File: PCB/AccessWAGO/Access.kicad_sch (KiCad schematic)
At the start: 82 parts, among them J1 USB-C, J2 NFC, J3 I/O, J4 TC2030-USB-NL-DS, J5 NFC, J6 GND, J7 12V, J8 DOOR, J9 I/O, Q2 PMF250XNEX, SW1 ESE13V01A, U1 MD8942, U10 ESP32-S3-MINI-1, U2 MD8942, U8 G3VM-41GR8

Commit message: Silkscreen, and 21
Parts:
- added J10: Reset, RevK:AA-Pad, symbol Connector_Generic:Conn_01x02
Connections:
- net GND: now also J10.1 (Pin_1)
- net at U10.25 (GPIO21): now also J10.2 (Pin_2)
- no-connect marks 25 -> 24
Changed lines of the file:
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@@
 	)
 	(no_connect
-		(at 39.37 102.87)
-	)
-	(no_connect
 		(at 39.37 69.85)
 	)
@@
 	(wire
 		(pts
+			(xy 30.48 102.87) (xy 39.37 102.87)
+		)
+		(stroke
+			(width 0)
+			(type default)
+		)
+	)
+	(wire
+		(pts
 			(xy 128.905 140.97) (xy 128.905 148.59)
 		)
@@
 	)
 	(symbol
+		(lib_id "power:GND")
+		(at 30.48 105.41 90)
+		(unit 1)
+		(exclude_from_sim no)
+		(in_bom yes)
+		(on_board yes)
+		(dnp no)
+		(fields_autoplaced yes)
+		(property "Reference" "#PWR09"
+			(at 36.83 105.41 0)
+			(effects
+				(font
+					(size 1.27 1.27)
+				)
+				(hide yes)
+			)
+		)
+		(property "Value" "GND"
+			(at 33.655 105.41 90)
+			(effects
+				(font
+					(size 1.27 1.27)
+				)
+				(justify right)
+			)
+		)
+		(property "Footprint" ""
+			(at 30.48 105.41 0)
+			(effects
+				(font
+					(size 1.27 1.27)
+				)
+				(hide yes)
+			)
+		)
+		(property "Datasheet" ""
+			(at 30.48 105.41 0)
+			(effects
+				(font
+					(size 1.27 1.27)
+				)
+				(hide yes)
+			)
+		)
+		(property "Description" "Power symbol creates a global label with name \"GND\" , ground"
+			(at 30.48 105.41 0)
+			(effects
+				(font
+					(size 1.27 1.27)
+				)
+				(hide yes)
+			)
+		)
+		(pin "1"
+		)
+		(instances
+			(project "Access"
+				(path "/2a267270-6585-45e3-a633-b53049f10066"
+					(reference "#PWR09")
+					(unit 1)
+				)
+			)
+		)
+	)
+	(symbol
 		(lib_id "power:+12V")
 		(at 175.26 50.8 90)
@@
 					(unit 1)
 				)
+			)
+		)
+	)
+	(symbol
+		(lib_id "Connector_Generic:Conn_01x02")
+		(at 25.4 105.41 180)
+		(unit 1)
+		(exclude_from_sim no)
+		(in_bom no)
+		(on_board yes)
+		(dnp no)
+		(fields_autoplaced yes)
+		(property "Reference" "J10"
+			(at 25.4 97.4555 0)
+			(effects
+				(font
+					(size 1.27 1.27)
+				)
+			)
+		)
+		(property "Value" "Reset"
+			(at 25.4 99.8798 0)
+			(effects
+				(font
+					(size 1.27 1.27)
+				)
+			)
+		)
+		(property "Footprint" "RevK:AA-Pad"
+			(at 25.4 105.41 0)
+			(effects
+				(font
+					(size 1.27 1.27)
+				)
+				(hide yes)
+			)
+		)
+		(property "Datasheet" "~"
+			(at 25.4 105.41 0)
+			(effects
+				(font
+					(size 1.27 1.27)
+				)
+				(hide yes)
+			)
+		)
+		(property "Description" "Generic connector, single row, 01x02, script generated (kicad-library-utils/schlib/autogen/connector/)"
+			(at 25.4 105.41 0)
+			(effects
+				(font
+					(size 1.27 1.27)
+				)
+				(hide yes)
+			)
+		)
+		(pin "2"
+		)
+		(pin "1"
+		)
+		(instances
+			(project "Access"
+				(path "/2a267270-6585-45e3-a633-b53049f10066"
+					(reference "J10")
+					(unit 1)
+				)

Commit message: Render
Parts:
- renumbered D4 to D11, D4 to D13, D4 to D14, D4 to D15, D4 to D16, D4 to D17, D4 to D18, D4 to D7
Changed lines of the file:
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@@
 (kicad_sch
-	(version 20231120)
+	(version 20241209)
 	(generator "eeschema")
-	(generator_version "8.0")
+	(generator_version "9.0")
 	(paper "A4")
 	(title_block
@@
 		(comment 2 "www.me.uk")
 	)
+	(text "Pulled up\nInverted"
+		(exclude_from_sim no)
+		(at 99.695 69.215 0)
+		(effects
+			(font
+				(size 1.27 1.27)
+			)
+			(justify left bottom)
+		)
+	)
 	(junction
 		(at 229.87 111.125)
@@
 		)
 	)
-	(text "Pulled up\nInverted"
-		(exclude_from_sim no)
-		(at 99.695 69.215 0)
-		(effects
-			(font
-				(size 1.27 1.27)
-			)
-			(justify left bottom)
-		)
-	)
 	(global_label "IO3"
 		(shape bidirectional)
@@
 		(on_board yes)
 		(dnp no)
-		(property "Reference" "D4"
+		(property "Reference" "D14"
 			(at 132.715 110.49 0)
 			(do_not_autoplace yes)
@@
 		(on_board yes)
 		(dnp no)
-		(property "Reference" "D4"
+		(property "Reference" "D7"
 			(at 68.58 130.81 0)
 			(do_not_autoplace yes)
@@
 		(dnp no)
 		(fields_autoplaced yes)
-		(property "Reference" "#PWR018"
+		(property "Reference" "#PWR011"
 			(at 62.738 130.81 0)
 			(effects
@@
 		(on_board yes)
 		(dnp no)
-		(property "Reference" "D4"
+		(property "Reference" "D13"
 			(at 132.715 95.25 0)
 			(do_not_autoplace yes)
@@
 		(dnp no)
 		(fields_autoplaced yes)
-		(property "Reference" "#PWR018"
+		(property "Reference" "#PWR036"
 			(at 136.525 91.44 0)
 			(effects
@@
 		(on_board yes)
 		(dnp no)
-		(property "Reference" "D4"
+		(property "Reference" "D17"
 			(at 132.715 155.956 0)
 			(do_not_autoplace yes)
@@
 		(on_board yes)
 		(dnp no)
-		(property "Reference" "D4"
+		(property "Reference" "D18"
 			(at 132.715 171.196 0)
 			(do_not_autoplace yes)
@@
 		(on_board yes)
 		(dnp no)
-		(property "Reference" "D4"
+		(property "Reference" "D16"
 			(at 132.715 140.97 0)
 			(do_not_autoplace yes)
@@
 		(on_board yes)
 		(dnp no)
-		(property "Reference" "D4"
+		(property "Reference" "D15"
 			(at 132.715 125.476 0)
 			(do_not_autoplace yes)
@@
 		(on_board yes)
 		(dnp no)
-		(property "Reference" "D4"
+		(property "Reference" "D11"
 			(at 81.28 130.81 0)
 			(do_not_autoplace yes)
@@
 		(dnp no)
 		(fields_autoplaced yes)
-		(property "Reference" "#PWR019"
+		(property "Reference" "#PWR012"
 			(at 62.738 140.97 0)
 			(effects
@@
 		(dnp no)
 		(fields_autoplaced yes)
-		(property "Reference" "#PWR019"
+		(property "Reference" "#PWR037"
 			(at 128.905 180.34 0)
 			(effects
@@
 		)
 	)
+	(embedded_fonts no)
 )

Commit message: PCB Update
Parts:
- C1, C21: LCSC Part # C194427 -> (none); MPN (none) -> C194427
- C15, C22: LCSC Part # C1691 -> (none); MPN (none) -> C1691
- D1, D10, D2, D3, D4, D6, D8, D9: LCSC Part # C5137770 -> (none); MPN (none) -> C5137770
- D11, D13, D14, D15, D16, D17, D18, D7: LCSC Part # C5349953 -> (none); MPN (none) -> C5349953
- D19, D5: LCSC Part # C5204746 -> (none); MPN (none) -> C5204746
- J1: LCSC Part # C709357 -> (none); MPN (none) -> C709357
- J2, J5, J8: LCSC Part # C2765055 -> (none); MPN (none) -> C2765055
- J3, J6, J7, J9: LCSC Part # C2765056 -> (none); MPN (none) -> C2765056
- Q2: JLCPCB Rotation Offset 0 -> (none); LCSC Part # C504047 -> (none); MPN (none) -> C504047
- U1, U2: LCSC Part # C2684786 -> (none); MPN (none) -> C2684786
- U10: LCSC Part # C3013941 -> (none); MPN (none) -> C3013941
- U8: JLCPCB Rotation Offset 180 -> (none); LCSC Part # C2691601 -> (none); MPN (none) -> C2691601
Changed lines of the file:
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@@
 			)
 		)
-		(property "LCSC Part #" "C709357"
+		(property "MPN" "C709357"
 			(at 127 44.45 0)
 			(effects
@@
 			)
 		)
-		(property "LCSC Part #" "C5137770"
+		(property "MPN" "C5137770"
 			(at 241.935 117.475 0)
 			(effects
@@
 			)
 		)
-		(property "LCSC Part #" "C5137770"
+		(property "MPN" "C5137770"
 			(at 156.21 144.78 0)
 			(effects
@@
 			)
 		)
-		(property "LCSC Part #" "C194427"
+		(property "MPN" "C194427"
 			(at 207.645 50.165 0)
 			(effects
@@
 			)
 		)
-		(property "LCSC Part #" "C5137770"
+		(property "MPN" "C5137770"
 			(at 156.21 114.3 0)
 			(effects
@@
 			)
 		)
-		(property "LCSC Part #" "C5349953"
+		(property "MPN" "C5349953"
 			(at 144.145 111.76 0)
 			(effects
@@
 			)
 		)
-		(property "LCSC Part #" "C5204746"
+		(property "MPN" "C5204746"
 			(at 250.825 80.645 0)
 			(effects
@@
 			)
 		)
-		(property "LCSC Part #" "C5349953"
+		(property "MPN" "C5349953"
 			(at 69.85 119.38 0)
 			(effects
@@
 			)
 		)
-		(property "LCSC Part #" "C2765056"
+		(property "MPN" "C2765056"
 			(at 259.715 135.89 0)
 			(effects
@@
 			)
 		)
-		(property "LCSC Part #" "C3013941"
+		(property "MPN" "C3013941"
 			(at 54.61 111.125 0)
 			(effects
@@
 			)
 		)
-		(property "LCSC Part #" "C2765056"
+		(property "MPN" "C2765056"
 			(at 259.715 78.105 0)
 			(effects
@@
 			)
 		)
-		(property "LCSC Part #" "C2691601"
-			(at 234.95 90.17 0)
-			(effects
-				(font
-					(size 1.27 1.27)
-				)
-				(hide yes)
-			)
-		)
-		(property "JLCPCB Rotation Offset" "180"
+		(property "MPN" "C2691601"
 			(at 234.95 90.17 0)
 			(effects
@@
 			)
 		)
-		(property "LCSC Part #" "C2765055"
+		(property "MPN" "C2765055"
 			(at 259.715 88.9 0)
 			(effects
@@
 			)
 		)
-		(property "LCSC Part #" "C2684786"
+		(property "MPN" "C2684786"
 			(at 186.69 56.515 0)
 			(effects
@@
 			)
 		)
-		(property "LCSC Part #" "C5349953"
+		(property "MPN" "C5349953"
 			(at 144.145 96.52 0)
 			(effects
@@
 			)
 		)
-		(property "LCSC Part #" "C5137770"
+		(property "MPN" "C5137770"
 			(at 156.21 99.06 0)
 			(effects
@@
 			)
 		)
-		(property "LCSC Part #" "C1691"
+		(property "MPN" "C1691"
 			(at 207.645 25.4 0)
 			(effects
@@
 			)
 		)
-		(property "LCSC Part #" "C5137770"
+		(property "MPN" "C5137770"
 			(at 156.21 129.54 0)
 			(effects
@@
 			)
 		)
-		(property "LCSC Part #" "C5349953"
+		(property "MPN" "C5349953"
 			(at 144.145 157.226 0)
 			(effects
@@
 			)
 		)
-		(property "LCSC Part #" "C5349953"
+		(property "MPN" "C5349953"
 			(at 144.145 172.466 0)
 			(effects
@@
 			)
 		)
-		(property "LCSC Part #" "C2765056"
+		(property "MPN" "C2765056"
 			(at 259.715 66.675 0)
 			(effects
@@
 			)
 		)
-		(property "LCSC Part #" "C2765056"
+		(property "MPN" "C2765056"
 			(at 259.715 143.51 0)
 			(effects
@@
 			)
 		)
-		(property "LCSC Part #" "C5137770"
+		(property "MPN" "C5137770"
 			(at 248.285 107.315 0)
 			(effects
@@
 			)
 		)
-		(property "LCSC Part #" "C5137770"
+		(property "MPN" "C5137770"
 			(at 156.21 175.26 0)
 			(effects
@@
 			)
 		)
-		(property "LCSC Part #" "C1691"
+		(property "MPN" "C1691"
 			(at 207.645 52.07 0)
 			(effects
@@
 			)
 		)
-		(property "LCSC Part #" "C5349953"
+		(property "MPN" "C5349953"
 			(at 144.145 142.24 0)
 			(effects
@@
 			)
 		)
-		(property "LCSC Part #" "C5349953"
+		(property "MPN" "C5349953"
 			(at 144.145 126.746 0)
 			(effects
@@
 			)
 		)
-		(property "LCSC Part #" "C5349953"
+		(property "MPN" "C5349953"
 			(at 82.55 119.38 0)
 			(effects
@@
 			)
 		)
-		(property "LCSC Part #" "C5137770"
+		(property "MPN" "C5137770"
 			(at 156.21 160.02 0)
 			(effects
@@
 			)
 		)
-		(property "LCSC Part #" "C5204746"
+		(property "MPN" "C5204746"
 			(at 268.605 20.955 0)
 			(effects
@@
 			)
 		)
-		(property "LCSC Part #" "C194427"
+		(property "MPN" "C194427"
 			(at 207.645 23.495 0)
 			(effects
@@
 			)
 		)
-		(property "LCSC Part #" "C504047"
-			(at 212.09 111.125 0)
-			(effects
-				(font
-					(size 1.27 1.27)
-				)
-				(hide yes)
-			)
-		)
-		(property "JLCPCB Rotation Offset" "0"
+		(property "MPN" "C504047"
 			(at 212.09 111.125 0)
 			(effects
@@
 			)
 		)
-		(property "LCSC Part #" "C2765055"
+		(property "MPN" "C2765055"
 			(at 259.715 106.045 0)
 			(effects
@@
 			)
 		)
-		(property "LCSC Part #" "C2684786"
+		(property "MPN" "C2684786"
 			(at 186.69 83.185 0)
 			(effects
@@
 			)
 		)
-		(property "LCSC Part #" "C2765055"
+		(property "MPN" "C2765055"
 			(at 259.715 111.125 0)
 			(effects

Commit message: Tidy
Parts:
- L3, L4: MPN (none) -> C42428017
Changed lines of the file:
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@@
 (kicad_sch
-	(version 20241209)
+	(version 20250114)
 	(generator "eeschema")
 	(generator_version "9.0")
@@
 			)
 		)
-		(property "Part No" ""
-			(at 207.645 61.595 0)
-			(effects
-				(font
-					(size 1.27 1.27)
-				)
-				(hide yes)
-			)
-		)
-		(property "Note" ""
-			(at 207.645 61.595 0)
+		(property "MPN" "C42428017"
+			(at 207.645 61.595 90)
 			(effects
 				(font
@@
 			)
 		)
-		(property "Part No" ""
-			(at 207.645 34.925 0)
-			(effects
-				(font
-					(size 1.27 1.27)
-				)
-				(hide yes)
-			)
-		)
-		(property "Note" ""
-			(at 207.645 34.925 0)
+		(property "MPN" "C42428017"
+			(at 207.645 34.925 90)
 			(effects
 				(font

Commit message: Component fix
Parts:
- L3, L4: MPN C42428017 -> C167879
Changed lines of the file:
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@@
 			)
 		)
-		(property "MPN" "C42428017"
+		(property "MPN" "C167879"
 			(at 207.645 61.595 90)
 			(effects
@@
 			)
 		)
-		(property "MPN" "C42428017"
+		(property "MPN" "C167879"
 			(at 207.645 34.925 90)
 			(effects

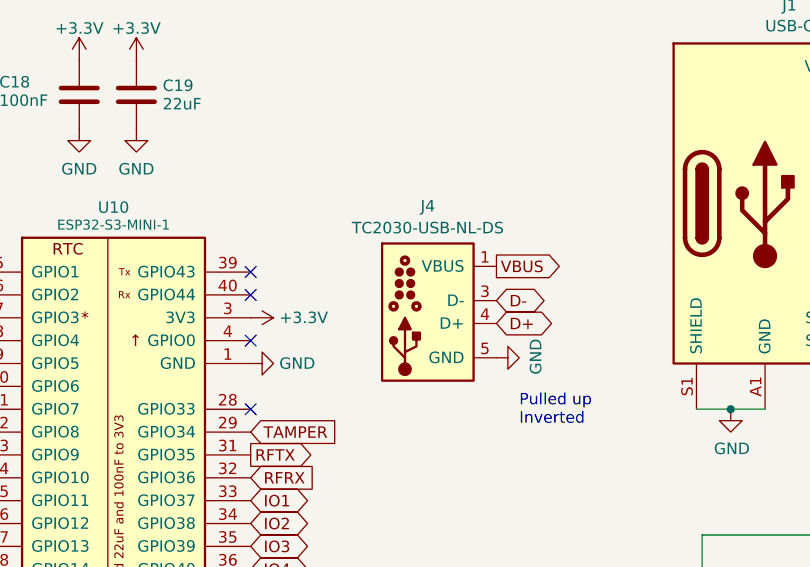
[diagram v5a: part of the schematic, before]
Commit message: Bell WAGO and other updates and renders
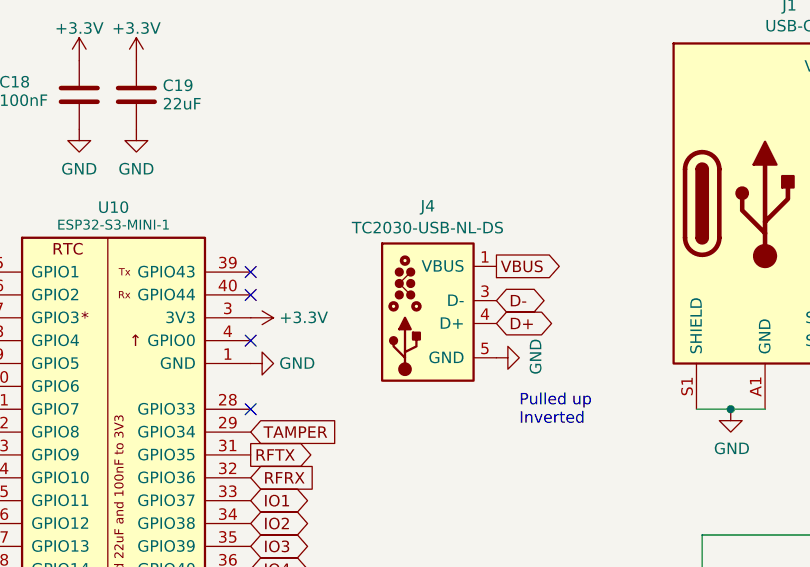
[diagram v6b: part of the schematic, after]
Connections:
- net D-: now also J4.2 (NC), J4.6 (NC)
- net GND: no longer J4.6 (GND)
- net VBUS: no longer J4.2 (VBUS)
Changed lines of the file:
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@@
 			)
 		)
-		(property "Datasheet" " ~"
+		(property "Datasheet" "~"
 			(at 93.345 57.785 0)
 			(effects
